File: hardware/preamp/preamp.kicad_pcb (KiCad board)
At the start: 2 copper layers, 45 x 17 mm, 32 parts, among them J1 I/O, J2 Conn 1, J3 Conn 2, Q1 2SC3324, Q2 2SC3324, U1 TLV170DBV

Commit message: Updated values
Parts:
- R12, R13: value 180k -> 200k
- R14: value 91k -> 100k
- R4, R7: value 1.5k -> 1k
- R5: value 13k -> 10k

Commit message: re-layout WIP
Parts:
- H1, H2, H3, H4: moved to F.Cu
- moved R5 5.21 mm to (144.7, 104.3)
- moved R4 4.99 mm to (142.3, 104.3)
- moved R12 4.99 mm to (146.6, 111.7), turned to 180 degrees
- moved R3 4.97 mm to (143.9, 109.2), turned to 0 degrees
- moved R13 4.94 mm to (146.6, 110.6), turned to 0 degrees
- moved R7 4.20 mm to (146.9, 104.3)
- moved D1 4.16 mm to (133.6, 101.2)
- moved C1 4.08 mm to (137.0, 101.2), turned to 0 degrees
- moved R8 3.90 mm to (142.2, 101.6), turned to 180 degrees
- moved R9 3.86 mm to (145.1, 101.6), turned to 180 degrees
- moved C2 3.07 mm to (139.6, 101.5), turned to 180 degrees
- moved JP1 3.06 mm to (142.2, 102.8)
- moved C3 2.74 mm to (143.1, 114.7), turned to 0 degrees
- moved R1 1.81 mm to (142.2, 102.7), turned to 180 degrees
- moved R11 1.71 mm to (145.9, 109.2), turned to 180 degrees
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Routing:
- net ext_coil+: track 29.0 -> 41.8 mm, vias 2 -> 4
- net GND: track 12.8 -> 25.2 mm, vias 16 -> 6
- net in-: track 11.5 -> 18.5 mm
- net V+: track 38.1 -> 45.1 mm, vias 0 -> 2
- net mix: track 12.9 -> 18.0 mm
- net Net-(R11-Pad2): track 7.03 -> 12.0 mm
- net out: track 15.2 -> 11.7 mm
- net ext_coil-: track 11.0 -> 14.2 mm
- net Net-(Q1-Pad2): track 4.56 -> 1.65 mm
- net Net-(Q1-Pad3): track 4.65 -> 2.50 mm
- net Net-(R4-Pad1): track 1.98 -> 4.11 mm
- net vcc: track 4.46 -> 2.68 mm
- net Net-(Q2-Pad3): track 4.26 -> 2.56 mm
- net Net-(Q2-Pad2): track 3.90 -> 2.45 mm
- net Net-(C3-Pad2): track 3.14 -> 3.73 mm
- removed copper zone on B.Cu, net ext_coil-
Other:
- board text added: "XR Spectra Preamp v1.01"
- board text removed: "XR Spectra Preamp v1.0"

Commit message: OK, this looks good
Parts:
- moved R12 0.65 mm to (145.9, 111.7)
- moved R13 0.65 mm to (145.9, 110.6)
- moved R14 0.65 mm to (145.9, 112.8)
- moved U1 0.65 mm to (142.8, 111.9)
- moved R7 0.60 mm to (146.3, 104.3)
- moved R5 0.40 mm to (144.3, 104.3)
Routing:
- net V+: track 45.1 -> 44.3 mm
- net Net-(Q2-Pad2): track 2.45 -> 1.94 mm

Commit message: cleanup
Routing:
- net GND: track 25.4 -> 14.6 mm, vias 6 -> 7
- net Net-(R11-Pad2): track 12.5 -> 13.5 mm
- removed copper zone on B.Cu, net in-

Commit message: Passive board updates
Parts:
- moved JP1 0.10 mm to (142.2, 102.7)

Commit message: updates for v1.01
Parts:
- moved J2 0.20 mm to (143.1, 108.5)

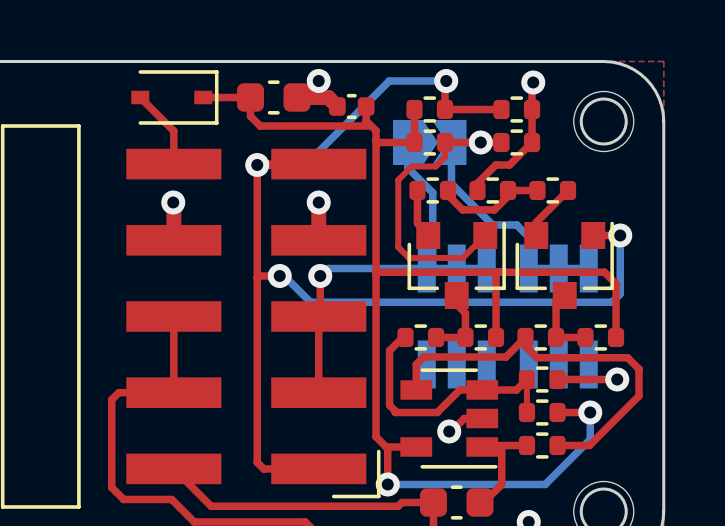
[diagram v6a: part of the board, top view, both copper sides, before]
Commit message: fix: reverse the 1mm connectors
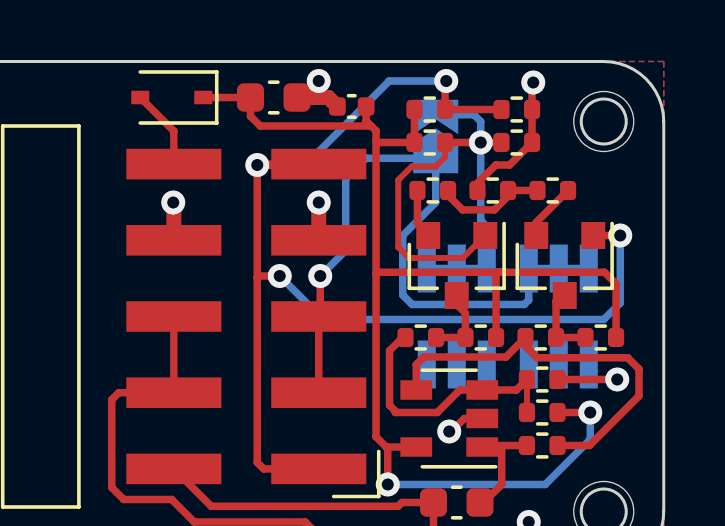
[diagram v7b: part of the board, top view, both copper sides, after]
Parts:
- moved J2 3.40 mm to (146.5, 108.5)
- moved J3 3.40 mm to (143.1, 108.5)
- moved JP1 0.28 mm to (142.4, 102.5), turned to 90 degrees
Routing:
- net ext_coil-: track 14.2 -> 23.3 mm
- net ext_coil+: track 41.8 -> 42.6 mm

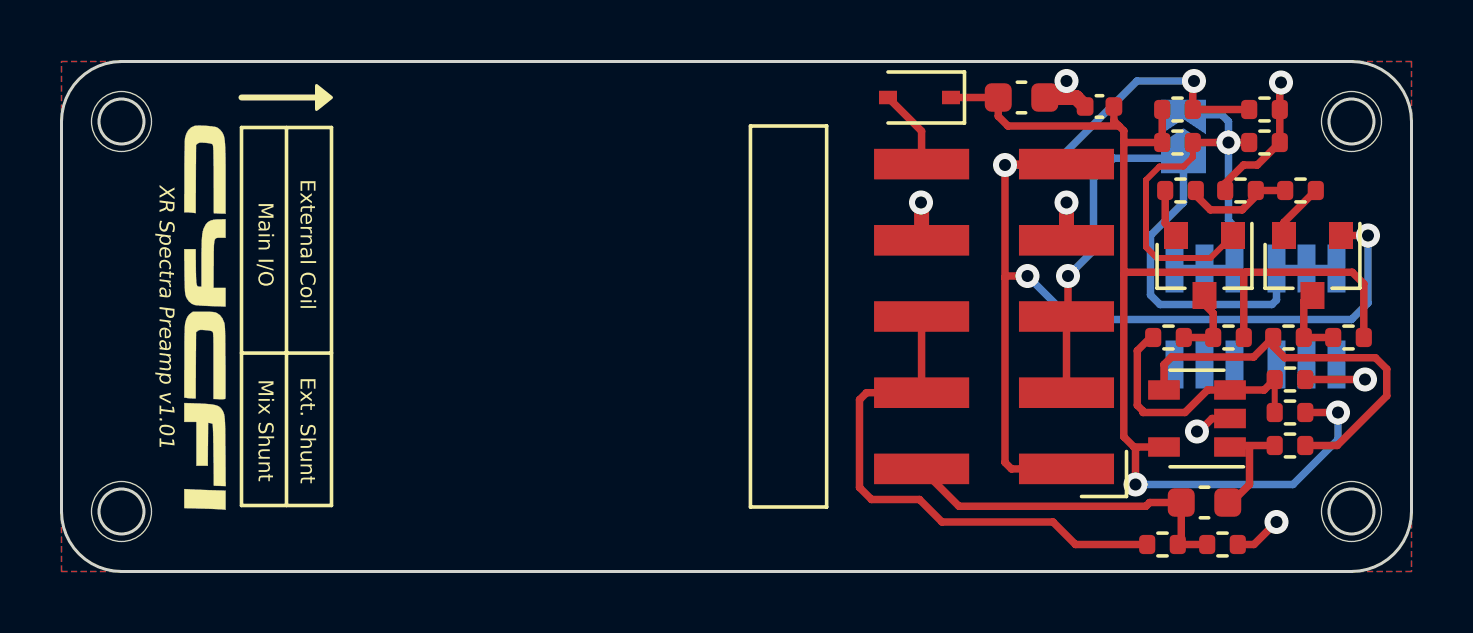
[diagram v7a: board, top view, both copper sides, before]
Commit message: Upgrade to Kicad 6 and cleanup files
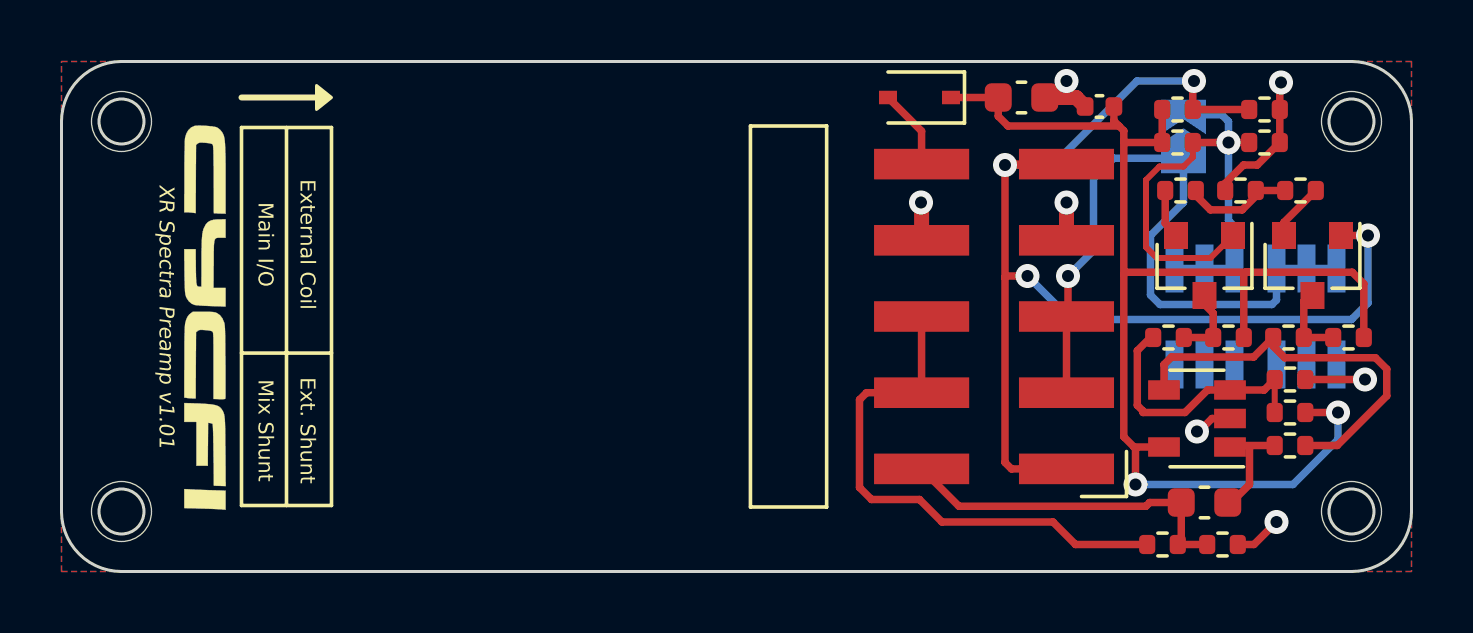
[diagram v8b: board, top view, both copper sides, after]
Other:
- net class Default removed
